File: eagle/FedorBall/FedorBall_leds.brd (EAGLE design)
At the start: 100 x 80 mm, 8 parts, among them U1 TLC5940-NT, U2 TLC5940-NT, U3 TLC5940-NT, U4 TLC5940-NT

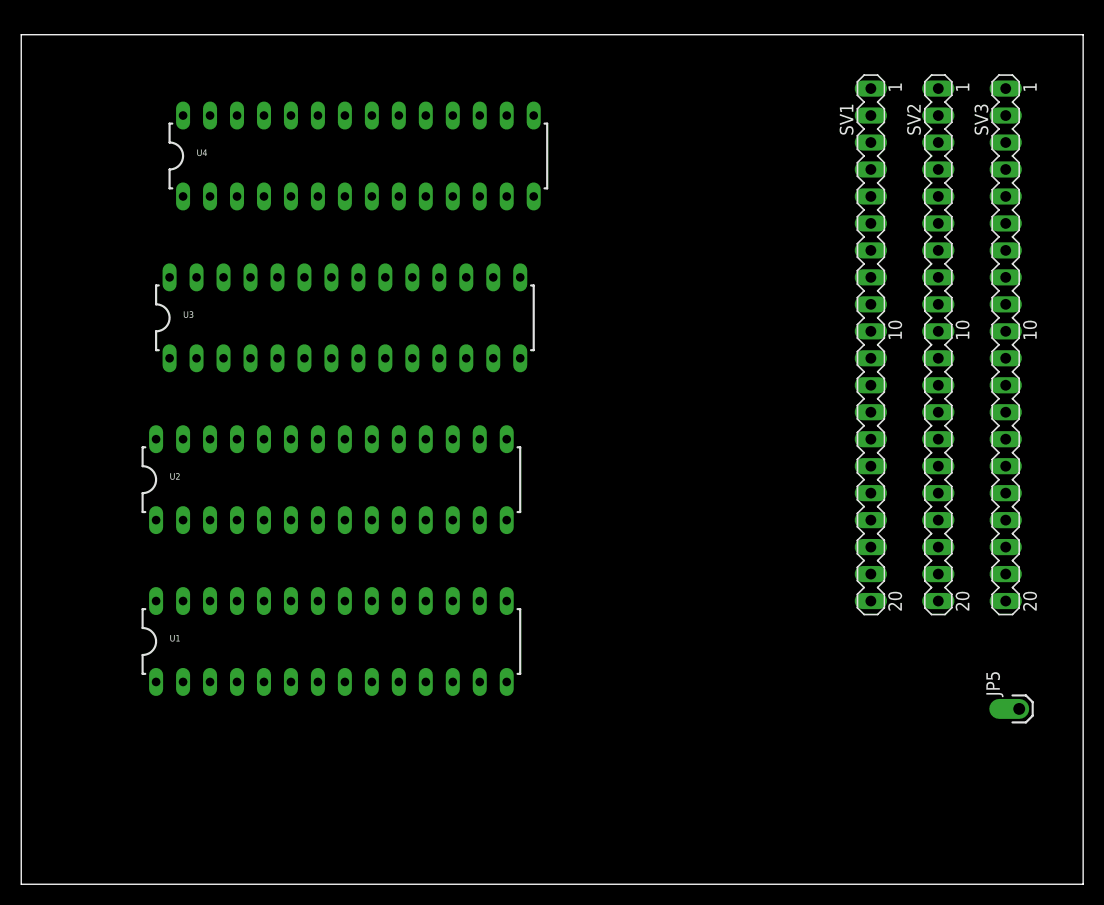
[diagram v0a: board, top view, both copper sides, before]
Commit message: continue implementing leds driver scheme
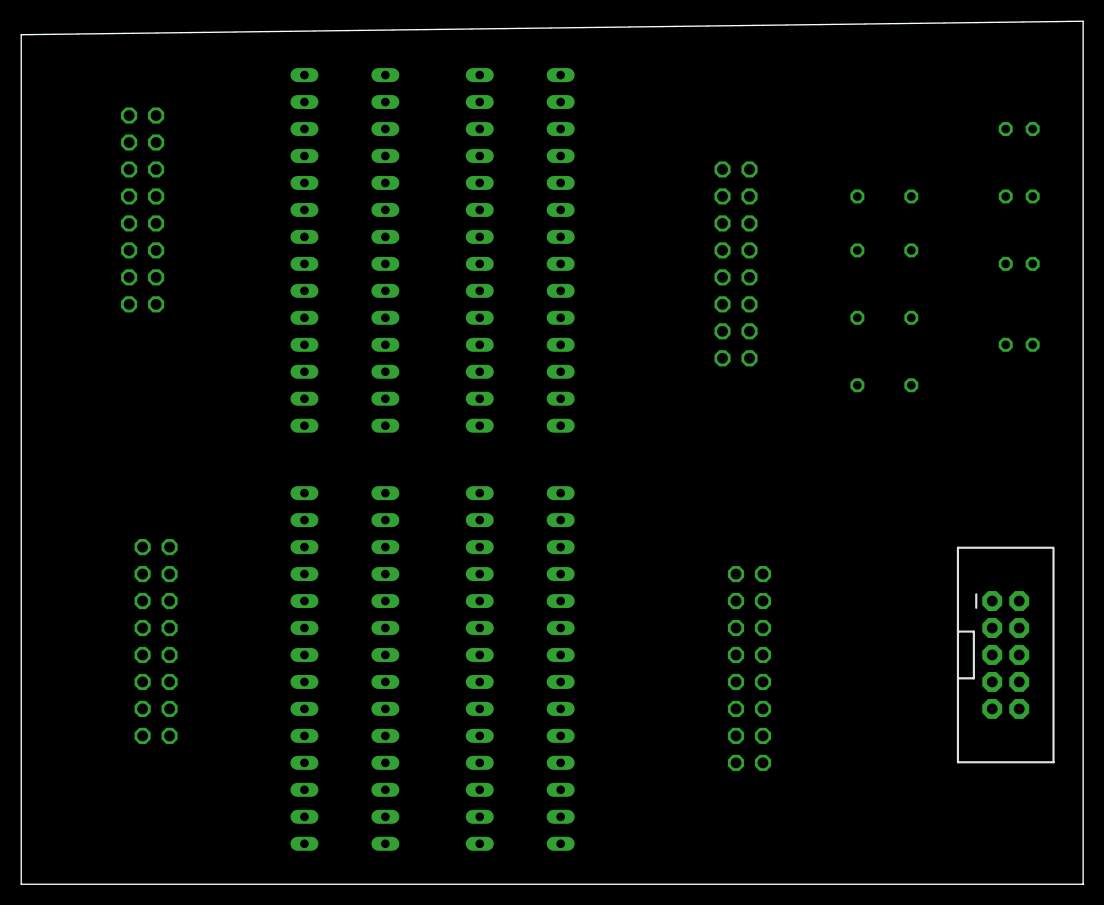
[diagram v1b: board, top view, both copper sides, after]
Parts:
- removed SV1, SV2, SV3: (no value), con-lstb:MA20-1L
- added C1, C2, C3, C4: 100n, rcl:C025-024X044
- added JP1: M05X2SHD, SparkFun:2X5-SHROUDED
- added JP3, JP4, JP6: (no value), pinhead:2X08
- added R1, R2, R3, R4: 2K, resistor:0204/5
- JP5: value M01OFFSET -> (none); device SparkFun:1X01_OFFSET -> pinhead:2X08
- moved JP5 81.5 mm to (12.7, 22.9), flipped to the bottom
- moved U1 40.9 mm to (47.0, 59.7), flipped to the bottom, turned to 90 degrees
- moved U3 33.0 mm to (30.5, 20.3), flipped to the bottom, turned to 90 degrees
- moved U2 25.1 mm to (47.0, 20.3), flipped to the bottom, turned to 90 degrees
- moved U4 8.98 mm to (30.5, 59.7), flipped to the bottom, turned to 90 degrees
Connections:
- removed net BUS_BLUE0: SV3.1
- removed net BUS_BLUE1: SV3.2
- removed net BUS_BLUE10: SV3.11
- removed net BUS_BLUE11: SV3.12
- removed net BUS_BLUE12: SV3.13
- removed net BUS_BLUE13: SV3.14
- removed net BUS_BLUE14: SV3.15
- removed net BUS_BLUE15: SV3.16
- removed net BUS_BLUE16: SV3.17
- removed net BUS_BLUE17: SV3.18
- removed net BUS_BLUE18: SV3.19
- removed net BUS_BLUE19: SV3.20
- removed net BUS_BLUE2: SV3.3
- removed net BUS_BLUE3: SV3.4
- removed net BUS_BLUE4: SV3.5, SV3.6
- removed net BUS_BLUE6: SV3.7
- removed net BUS_BLUE7: SV3.8
- removed net BUS_BLUE8: SV3.9
- removed net BUS_BLUE9: SV3.10
- removed net BUS_GREEN0: SV2.1
- removed net BUS_GREEN1: SV2.2
- removed net BUS_GREEN10: SV2.11
- removed net BUS_GREEN11: SV2.12
- removed net BUS_GREEN12: SV2.13
- removed net BUS_GREEN13: SV2.14
- removed net BUS_GREEN14: SV2.15
- removed net BUS_GREEN15: SV2.16
- removed net BUS_GREEN16: SV2.17
- removed net BUS_GREEN17: SV2.18
- removed net BUS_GREEN18: SV2.19
- removed net BUS_GREEN19: SV2.20
- removed net BUS_GREEN3: SV2.3, SV2.4
- removed net BUS_GREEN4: SV2.5
- removed net BUS_GREEN5: SV2.6
- removed net BUS_GREEN6: SV2.7
- removed net BUS_GREEN7: SV2.8
- removed net BUS_GREEN8: SV2.9
- removed net BUS_GREEN9: SV2.10
- removed net BUS_RED0: SV1.1
- removed net BUS_RED1: SV1.2
- removed net BUS_RED10: SV1.11
- removed net BUS_RED11: SV1.12
- removed net BUS_RED12: SV1.13
- removed net BUS_RED13: SV1.14
- removed net BUS_RED14: SV1.15
- removed net BUS_RED15: SV1.16
- removed net BUS_RED16: SV1.17
- removed net BUS_RED17: SV1.18
- removed net BUS_RED18: SV1.19
- removed net BUS_RED19: SV1.20
- removed net BUS_RED2: SV1.3
- removed net BUS_RED3: SV1.4
- removed net BUS_RED4: SV1.5
- removed net BUS_RED5: SV1.6
- removed net BUS_RED6: SV1.7
- removed net BUS_RED7: SV1.8
- removed net BUS_RED8: SV1.9
- removed net BUS_RED9: SV1.10
- new net +5V: C1.1, C2.1, C3.1, C4.1, JP1.10, JP3.16, JP4.16, JP5.16, JP6.16, U1.21, U2.21, U3.21, U4.21
- new net DRIVERS_BUS0: JP1.2, U1.23, U2.23, U3.23, U4.23
- new net DRIVERS_BUS1: JP1.1, U1.25, U2.25, U3.25
- new net DRIVERS_BUS2: JP1.5, U1.26
- new net DRIVERS_BUS3: JP1.3, U4.17
- new net DRIVERS_BUS4: JP1.7, U1.24, U2.24, U3.24, U4.24
- new net DRIVERS_BUS5: JP1.4, U1.18, U2.18, U3.18, U4.18
- new net DRIVERS_BUS6: JP1.8, U1.19, U2.19, U3.19, U4.19
- new net DRIVERS_BUS7: JP1.6, U1.27, U2.27, U3.27, U4.27
- new net LEDS_BUS0: JP3.1, U1.28
- new net LEDS_BUS1: JP3.3, U1.1
- new net LEDS_BUS10: JP3.6, U1.10
- new net LEDS_BUS11: JP3.8, U1.11
- new net LEDS_BUS12: JP3.10, U1.12
- new net LEDS_BUS13: JP3.12, U1.13
- new net LEDS_BUS14: JP3.14, U1.14
- new net LEDS_BUS15: JP4.1, U2.28
- new net LEDS_BUS16: JP4.3, U2.1
- new net LEDS_BUS17: JP4.5, U2.2
- new net LEDS_BUS18: JP4.7, U2.3
- new net LEDS_BUS19: JP4.9, U2.4
- new net LEDS_BUS2: JP3.5, U1.2
- new net LEDS_BUS20: JP4.11, U2.5
- new net LEDS_BUS21: JP4.13, U2.6
- new net LEDS_BUS22: JP4.15, U2.7
- new net LEDS_BUS23: JP4.2, U2.8
- new net LEDS_BUS24: JP4.4, U2.9
- new net LEDS_BUS25: JP4.6, U2.10
- new net LEDS_BUS26: JP4.8, U2.11
- new net LEDS_BUS27: JP4.10, U2.12
- new net LEDS_BUS28: JP4.12, U2.13
- new net LEDS_BUS29: JP4.14, U2.14
- new net LEDS_BUS3: JP3.7, U1.3
- new net LEDS_BUS30: JP5.1, U3.28
- new net LEDS_BUS31: JP5.3, U3.1
- new net LEDS_BUS32: JP5.5, U3.2
- new net LEDS_BUS33: JP5.7, U3.3
- new net LEDS_BUS34: JP5.9, U3.4
- new net LEDS_BUS35: JP5.11, U3.5
- new net LEDS_BUS36: JP5.13, U3.6
- new net LEDS_BUS37: JP5.15, U3.7
- new net LEDS_BUS38: JP5.2, U3.8
- new net LEDS_BUS39: JP5.4, U3.9
- new net LEDS_BUS4: JP3.9, U1.4
- new net LEDS_BUS40: JP5.6, U3.10
- new net LEDS_BUS41: JP5.8, U3.11
- new net LEDS_BUS42: JP5.10, U3.12
- new net LEDS_BUS43: JP5.12, U3.13
- new net LEDS_BUS44: JP5.14, U3.14
- new net LEDS_BUS45: JP6.1, U4.28
- new net LEDS_BUS46: JP6.3, U4.1
- new net LEDS_BUS47: JP6.5, U4.2
- new net LEDS_BUS48: JP6.7, U4.3
- new net LEDS_BUS49: JP6.9, U4.4
- new net LEDS_BUS5: JP3.11, U1.5
- new net LEDS_BUS50: JP6.11, U4.5
- new net LEDS_BUS51: JP6.13, U4.6
- new net LEDS_BUS52: JP6.15, U4.7
- new net LEDS_BUS53: JP6.2, U4.8
- new net LEDS_BUS54: JP6.4, U4.9
- new net LEDS_BUS55: JP6.6, U4.10
- new net LEDS_BUS56: JP6.8, U4.11
- new net LEDS_BUS57: JP6.10, U4.12
- new net LEDS_BUS58: JP6.12, U4.13
- new net LEDS_BUS59: JP6.14, U4.14
- new net LEDS_BUS6: JP3.13, U1.6
- new net LEDS_BUS7: JP3.15, U1.7
- new net LEDS_BUS8: JP3.2, U1.8
- new net LEDS_BUS9: JP3.4, U1.9
- new net N$1: U1.17, U2.26
- new net N$2: U2.17, U3.26
- new net N$3: U3.17, U4.26
- new net N$4: R2.2, U1.20
- new net N$5: R4.2, U2.20
- new net N$6: R3.2, U3.20
- new net N$7: R1.2, U4.20
- net GND: now also C1.2, C2.2, C3.2, C4.2, JP1.9, R1.1, R2.1, R3.1, R4.1, U1.22, U2.22, U3.22, U4.22; no longer JP5.1
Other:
- board size 100 x 80 mm -> 100 x 81.3 mm

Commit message: update scheme
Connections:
- net +5V: now also JP1.2; no longer JP1.10
- net DRIVERS_BUS0: now also JP1.6; no longer JP1.2
- net DRIVERS_BUS1: now also JP1.10; no longer JP1.1
- net DRIVERS_BUS2: now also JP1.9; no longer JP1.5
- net DRIVERS_BUS3: now also JP1.8; no longer JP1.3
- net DRIVERS_BUS4: now also JP1.3; no longer JP1.7
- net DRIVERS_BUS5: now also JP1.7; no longer JP1.4
- net DRIVERS_BUS6: now also JP1.4; no longer JP1.8
- net DRIVERS_BUS7: now also JP1.5; no longer JP1.6
- net GND: now also JP1.1; no longer JP1.9
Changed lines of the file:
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@@
 <contactref element="U3" pad="21"/>
 <contactref element="U4" pad="21"/>
-<contactref element="JP1" pad="10"/>
 <contactref element="C1" pad="1"/>
 <contactref element="C2" pad="1"/>
 <contactref element="C3" pad="1"/>
 <contactref element="C4" pad="1"/>
+<contactref element="JP1" pad="2"/>
+<wire x1="95.25" y1="64.77" x2="95.25" y2="71.12" width="0" layer="19" extent="1-1"/>
+<wire x1="95.25" y1="58.42" x2="95.25" y2="64.77" width="0" layer="19" extent="1-1"/>
+<wire x1="95.25" y1="50.8" x2="95.25" y2="58.42" width="0" layer="19" extent="1-1"/>
+<wire x1="93.98" y1="26.67" x2="95.25" y2="50.8" width="0" layer="19" extent="1-1"/>
+<wire x1="69.85" y1="29.21" x2="93.98" y2="26.67" width="0" layer="19" extent="1-1"/>
+<wire x1="50.8" y1="21.59" x2="69.85" y2="29.21" width="0" layer="19" extent="1-1"/>
+<wire x1="34.29" y1="21.59" x2="50.8" y2="21.59" width="0" layer="19" extent="1-1"/>
+<wire x1="13.97" y1="31.75" x2="34.29" y2="21.59" width="0" layer="19" extent="1-1"/>
+<wire x1="68.58" y1="67.31" x2="95.25" y2="64.77" width="0" layer="19" extent="1-1"/>
 <wire x1="50.8" y1="60.96" x2="68.58" y2="67.31" width="0" layer="19" extent="1-1"/>
 <wire x1="34.29" y1="60.96" x2="50.8" y2="60.96" width="0" layer="19" extent="1-1"/>
 <wire x1="12.7" y1="72.39" x2="34.29" y2="60.96" width="0" layer="19" extent="1-1"/>
-<wire x1="95.25" y1="71.12" x2="50.8" y2="60.96" width="0" layer="19" extent="1-1"/>
-<wire x1="95.25" y1="64.77" x2="95.25" y2="71.12" width="0" layer="19" extent="1-1"/>
-<wire x1="95.25" y1="58.42" x2="95.25" y2="64.77" width="0" layer="19" extent="1-1"/>
-<wire x1="95.25" y1="50.8" x2="95.25" y2="58.42" width="0" layer="19" extent="1-1"/>
-<wire x1="50.8" y1="21.59" x2="95.25" y2="58.42" width="0" layer="19" extent="1-1"/>
-<wire x1="34.29" y1="21.59" x2="50.8" y2="21.59" width="0" layer="19" extent="1-1"/>
-<wire x1="13.97" y1="31.75" x2="34.29" y2="21.59" width="0" layer="19" extent="1-1"/>
-<wire x1="93.98" y1="16.51" x2="95.25" y2="50.8" width="0" layer="19" extent="1-1"/>
 </signal>
 <signal name="N$1">
@@
 <contactref element="R3" pad="1"/>
 <contactref element="R1" pad="1"/>
-<contactref element="JP1" pad="9"/>
 <contactref element="C1" pad="2"/>
 <contactref element="C2" pad="2"/>
 <contactref element="C3" pad="2"/>
 <contactref element="C4" pad="2"/>
-<wire x1="34.29" y1="58.42" x2="50.8" y2="58.42" width="0" layer="19" extent="1-1"/>
-<wire x1="92.71" y1="71.12" x2="50.8" y2="58.42" width="0" layer="19" extent="1-1"/>
+<contactref element="JP1" pad="1"/>
 <wire x1="92.71" y1="64.77" x2="92.71" y2="71.12" width="0" layer="19" extent="1-1"/>
 <wire x1="92.71" y1="58.42" x2="92.71" y2="64.77" width="0" layer="19" extent="1-1"/>
@@
 <wire x1="78.74" y1="59.69" x2="78.74" y2="64.77" width="0" layer="19" extent="1-1"/>
 <wire x1="78.74" y1="53.34" x2="78.74" y2="59.69" width="0" layer="19" extent="1-1"/>
-<wire x1="50.8" y1="19.05" x2="78.74" y2="53.34" width="0" layer="19" extent="1-1"/>
 <wire x1="78.74" y1="46.99" x2="78.74" y2="53.34" width="0" layer="19" extent="1-1"/>
+<wire x1="91.44" y1="26.67" x2="78.74" y2="46.99" width="0" layer="19" extent="1-1"/>
+<wire x1="50.8" y1="58.42" x2="78.74" y2="59.69" width="0" layer="19" extent="1-1"/>
+<wire x1="34.29" y1="58.42" x2="50.8" y2="58.42" width="0" layer="19" extent="1-1"/>
+<wire x1="50.8" y1="19.05" x2="50.8" y2="58.42" width="0" layer="19" extent="1-1"/>
 <wire x1="34.29" y1="19.05" x2="50.8" y2="19.05" width="0" layer="19" extent="1-1"/>
-<wire x1="91.44" y1="16.51" x2="92.71" y2="50.8" width="0" layer="19" extent="1-1"/>
 </signal>
 <signal name="N$5">
@@
 <contactref element="U3" pad="23"/>
 <contactref element="U4" pad="23"/>
-<contactref element="JP1" pad="2"/>
-<wire x1="50.8" y1="16.51" x2="93.98" y2="26.67" width="0" layer="19" extent="1-1"/>
+<contactref element="JP1" pad="6"/>
+<wire x1="50.8" y1="16.51" x2="93.98" y2="21.59" width="0" layer="19" extent="1-1"/>
 <wire x1="34.29" y1="16.51" x2="50.8" y2="16.51" width="0" layer="19" extent="1-1"/>
 <wire x1="50.8" y1="55.88" x2="50.8" y2="16.51" width="0" layer="19" extent="1-1"/>
@@
 <contactref element="U2" pad="25"/>
 <contactref element="U3" pad="25"/>
-<contactref element="JP1" pad="1"/>
-<wire x1="50.8" y1="11.43" x2="91.44" y2="26.67" width="0" layer="19" extent="1-1"/>
+<contactref element="JP1" pad="10"/>
+<wire x1="50.8" y1="11.43" x2="93.98" y2="16.51" width="0" layer="19" extent="1-1"/>
 <wire x1="34.29" y1="11.43" x2="50.8" y2="11.43" width="0" layer="19" extent="1-1"/>
 <wire x1="50.8" y1="50.8" x2="50.8" y2="11.43" width="0" layer="19" extent="1-1"/>
@@
 <signal name="DRIVERS_BUS2">
 <contactref element="U1" pad="26"/>
-<contactref element="JP1" pad="5"/>
-<wire x1="50.8" y1="48.26" x2="91.44" y2="21.59" width="0" layer="19" extent="1-1"/>
+<contactref element="JP1" pad="9"/>
+<wire x1="50.8" y1="48.26" x2="91.44" y2="16.51" width="0" layer="19" extent="1-1"/>
 </signal>
 <signal name="DRIVERS_BUS3">
 <contactref element="U4" pad="17"/>
-<contactref element="JP1" pad="3"/>
-<wire x1="34.29" y1="71.12" x2="91.44" y2="24.13" width="0" layer="19" extent="1-1"/>
+<contactref element="JP1" pad="8"/>
+<wire x1="34.29" y1="71.12" x2="93.98" y2="19.05" width="0" layer="19" extent="1-1"/>
 </signal>
 <signal name="DRIVERS_BUS4">
@@
 <contactref element="U3" pad="24"/>
 <contactref element="U4" pad="24"/>
-<contactref element="JP1" pad="7"/>
+<contactref element="JP1" pad="3"/>
+<wire x1="50.8" y1="13.97" x2="91.44" y2="24.13" width="0" layer="19" extent="1-1"/>
+<wire x1="34.29" y1="13.97" x2="50.8" y2="13.97" width="0" layer="19" extent="1-1"/>
+<wire x1="50.8" y1="53.34" x2="50.8" y2="13.97" width="0" layer="19" extent="1-1"/>
 <wire x1="34.29" y1="53.34" x2="50.8" y2="53.34" width="0" layer="19" extent="1-1"/>
-<wire x1="50.8" y1="13.97" x2="50.8" y2="53.34" width="0" layer="19" extent="1-1"/>
-<wire x1="34.29" y1="13.97" x2="50.8" y2="13.97" width="0" layer="19" extent="1-1"/>
-<wire x1="91.44" y1="19.05" x2="50.8" y2="13.97" width="0" layer="19" extent="1-1"/>
 </signal>
 <signal name="DRIVERS_BUS5">
@@
 <contactref element="U3" pad="18"/>
 <contactref element="U4" pad="18"/>
-<contactref element="JP1" pad="4"/>
+<contactref element="JP1" pad="7"/>
 <wire x1="34.29" y1="68.58" x2="50.8" y2="68.58" width="0" layer="19" extent="1-1"/>
 <wire x1="50.8" y1="29.21" x2="50.8" y2="68.58" width="0" layer="19" extent="1-1"/>
 <wire x1="34.29" y1="29.21" x2="50.8" y2="29.21" width="0" layer="19" extent="1-1"/>
-<wire x1="93.98" y1="24.13" x2="50.8" y2="29.21" width="0" layer="19" extent="1-1"/>
+<wire x1="91.44" y1="19.05" x2="50.8" y2="29.21" width="0" layer="19" extent="1-1"/>
 </signal>
 <signal name="DRIVERS_BUS6">
@@
 <contactref element="U3" pad="19"/>
 <contactref element="U4" pad="19"/>
-<contactref element="JP1" pad="8"/>
+<contactref element="JP1" pad="4"/>
 <wire x1="34.29" y1="66.04" x2="50.8" y2="66.04" width="0" layer="19" extent="1-1"/>
 <wire x1="50.8" y1="26.67" x2="50.8" y2="66.04" width="0" layer="19" extent="1-1"/>
 <wire x1="34.29" y1="26.67" x2="50.8" y2="26.67" width="0" layer="19" extent="1-1"/>
-<wire x1="93.98" y1="19.05" x2="50.8" y2="26.67" width="0" layer="19" extent="1-1"/>
+<wire x1="93.98" y1="24.13" x2="50.8" y2="26.67" width="0" layer="19" extent="1-1"/>
 </signal>
 <signal name="DRIVERS_BUS7">
@@
 <contactref element="U3" pad="27"/>
 <contactref element="U4" pad="27"/>
-<contactref element="JP1" pad="6"/>
-<wire x1="50.8" y1="6.35" x2="93.98" y2="21.59" width="0" layer="19" extent="1-1"/>
+<contactref element="JP1" pad="5"/>
+<wire x1="50.8" y1="6.35" x2="91.44" y2="21.59" width="0" layer="19" extent="1-1"/>
 <wire x1="34.29" y1="6.35" x2="50.8" y2="6.35" width="0" layer="19" extent="1-1"/>
 <wire x1="50.8" y1="45.72" x2="50.8" y2="6.35" width="0" layer="19" extent="1-1"/>

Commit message: update leds board scheme
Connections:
- removed net LEDS_BUS0: JP3.1, U1.28
- removed net LEDS_BUS1: JP3.3, U1.1
- removed net LEDS_BUS10: JP3.6, U1.10
- removed net LEDS_BUS11: JP3.8, U1.11
- removed net LEDS_BUS12: JP3.10, U1.12
- removed net LEDS_BUS13: JP3.12, U1.13
- removed net LEDS_BUS14: JP3.14, U1.14
- removed net LEDS_BUS15: JP4.1, U2.28
- removed net LEDS_BUS16: JP4.3, U2.1
- removed net LEDS_BUS17: JP4.5, U2.2
- removed net LEDS_BUS18: JP4.7, U2.3
- removed net LEDS_BUS19: JP4.9, U2.4
- removed net LEDS_BUS2: JP3.5, U1.2
- removed net LEDS_BUS20: JP4.11, U2.5
- removed net LEDS_BUS21: JP4.13, U2.6
- removed net LEDS_BUS22: JP4.15, U2.7
- removed net LEDS_BUS23: JP4.2, U2.8
- removed net LEDS_BUS24: JP4.4, U2.9
- removed net LEDS_BUS25: JP4.6, U2.10
- removed net LEDS_BUS26: JP4.8, U2.11
- removed net LEDS_BUS27: JP4.10, U2.12
- removed net LEDS_BUS28: JP4.12, U2.13
- removed net LEDS_BUS29: JP4.14, U2.14
- removed net LEDS_BUS3: JP3.7, U1.3
- removed net LEDS_BUS30: JP5.1, U3.28
- removed net LEDS_BUS31: JP5.3, U3.1
- removed net LEDS_BUS32: JP5.5, U3.2
- removed net LEDS_BUS33: JP5.7, U3.3
- removed net LEDS_BUS34: JP5.9, U3.4
- removed net LEDS_BUS35: JP5.11, U3.5
- removed net LEDS_BUS36: JP5.13, U3.6
- removed net LEDS_BUS37: JP5.15, U3.7
- removed net LEDS_BUS38: JP5.2, U3.8
- removed net LEDS_BUS39: JP5.4, U3.9
- removed net LEDS_BUS4: JP3.9, U1.4
- removed net LEDS_BUS40: JP5.6, U3.10
- removed net LEDS_BUS41: JP5.8, U3.11
- removed net LEDS_BUS42: JP5.10, U3.12
- removed net LEDS_BUS43: JP5.12, U3.13
- removed net LEDS_BUS44: JP5.14, U3.14
- removed net LEDS_BUS45: JP6.1, U4.28
- removed net LEDS_BUS46: JP6.3, U4.1
- removed net LEDS_BUS47: JP6.5, U4.2
- removed net LEDS_BUS48: JP6.7, U4.3
- removed net LEDS_BUS49: JP6.9, U4.4
- removed net LEDS_BUS5: JP3.11, U1.5
- removed net LEDS_BUS50: JP6.11, U4.5
- removed net LEDS_BUS51: JP6.13, U4.6
- removed net LEDS_BUS52: JP6.15, U4.7
- removed net LEDS_BUS53: JP6.2, U4.8
- removed net LEDS_BUS54: JP6.4, U4.9
- removed net LEDS_BUS55: JP6.6, U4.10
- removed net LEDS_BUS56: JP6.8, U4.11
- removed net LEDS_BUS57: JP6.10, U4.12
- removed net LEDS_BUS58: JP6.12, U4.13
- removed net LEDS_BUS59: JP6.14, U4.14
- removed net LEDS_BUS6: JP3.13, U1.6
- removed net LEDS_BUS7: JP3.15, U1.7
- removed net LEDS_BUS8: JP3.2, U1.8
- removed net LEDS_BUS9: JP3.4, U1.9
- new net LEDS0_0: JP3.16, U1.1
- new net LEDS0_1: JP3.15, U1.2
- new net LEDS0_10: JP3.6, U1.11
- new net LEDS0_11: JP3.5, U1.12
- new net LEDS0_12: JP3.4, U1.13
- new net LEDS0_13: JP3.3, U1.14
- new net LEDS0_14: JP3.2, U1.15
- new net LEDS0_2: JP3.14, U1.3
- new net LEDS0_3: JP3.13, U1.4
- new net LEDS0_4: JP3.12, U1.5
- new net LEDS0_5: JP3.11, U1.6
- new net LEDS0_6: JP3.10, U1.7
- new net LEDS0_7: JP3.9, U1.8
- new net LEDS0_8: JP3.8, U1.9
- new net LEDS0_9: JP3.7, U1.10
- new net LEDS1_0: JP4.16, U2.1
- new net LEDS1_1: JP4.15, U2.2
- new net LEDS1_10: JP4.6, U2.11
- new net LEDS1_11: JP4.5, U2.12
- new net LEDS1_12: JP4.4, U2.13
- new net LEDS1_13: JP4.3, U2.14
- new net LEDS1_14: JP4.2, U2.15
- new net LEDS1_2: JP4.14, U2.3
- new net LEDS1_3: JP4.13, U2.4
- new net LEDS1_4: JP4.12, U2.5
- new net LEDS1_5: JP4.11, U2.6
- new net LEDS1_6: JP4.10, U2.7
- new net LEDS1_7: JP4.9, U2.8
- new net LEDS1_8: JP4.8, U2.9
- new net LEDS1_9: JP4.7, U2.10
- new net LEDS2_0: JP5.16, U3.1
- new net LEDS2_1: JP5.15, U3.2
- new net LEDS2_10: JP5.6, U3.11
- new net LEDS2_11: JP5.5, U3.12
- new net LEDS2_12: JP5.4, U3.13
- new net LEDS2_13: JP5.3, U3.14
- new net LEDS2_14: JP5.2, U3.15
- new net LEDS2_2: JP5.14, U3.3
- new net LEDS2_3: JP5.13, U3.4
- new net LEDS2_4: JP5.12, U3.5
- new net LEDS2_5: JP5.11, U3.6
- new net LEDS2_6: JP5.10, U3.7
- new net LEDS2_7: JP5.9, U3.8
- new net LEDS2_8: JP5.8, U3.9
- new net LEDS2_9: JP5.7, U3.10
- new net LEDS3_0: JP6.16, U4.1
- new net LEDS3_1: JP6.15, U4.2
- new net LEDS3_10: JP6.6, U4.11
- new net LEDS3_11: JP6.5, U4.12
- new net LEDS3_12: JP6.4, U4.13
- new net LEDS3_13: JP6.3, U4.14
- new net LEDS3_14: JP6.2, U4.15
- new net LEDS3_2: JP6.14, U4.3
- new net LEDS3_3: U4.4
- new net LEDS3_4: JP6.12, U4.5
- new net LEDS3_5: JP6.11, U4.6
- new net LEDS3_6: JP6.10, U4.7
- new net LEDS3_7: JP6.9, U4.8
- new net LEDS3_8: JP6.8, U4.9
- new net LEDS3_9: JP6.7, U4.10
- net +5V: now also JP1.9, JP3.1, JP4.1, JP5.1, JP6.1; no longer JP1.2, JP3.16, JP4.16, JP5.16, JP6.16
- net DRIVERS_BUS0: now also JP1.5; no longer JP1.6
- net DRIVERS_BUS1: now also JP1.1; no longer JP1.10
- net DRIVERS_BUS2: now also JP1.2; no longer JP1.9
- net DRIVERS_BUS3: now also JP1.3; no longer JP1.8
- net DRIVERS_BUS4: now also JP1.8; no longer JP1.3
- net DRIVERS_BUS5: now also JP1.4; no longer JP1.7
- net DRIVERS_BUS6: now also JP1.7; no longer JP1.4
- net DRIVERS_BUS7: now also JP1.6; no longer JP1.5
- net GND: now also JP1.10; no longer JP1.1
